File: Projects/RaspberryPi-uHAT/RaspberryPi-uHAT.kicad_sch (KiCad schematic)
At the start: 6 parts, among them J1 GPIO, U1 CAT24C256

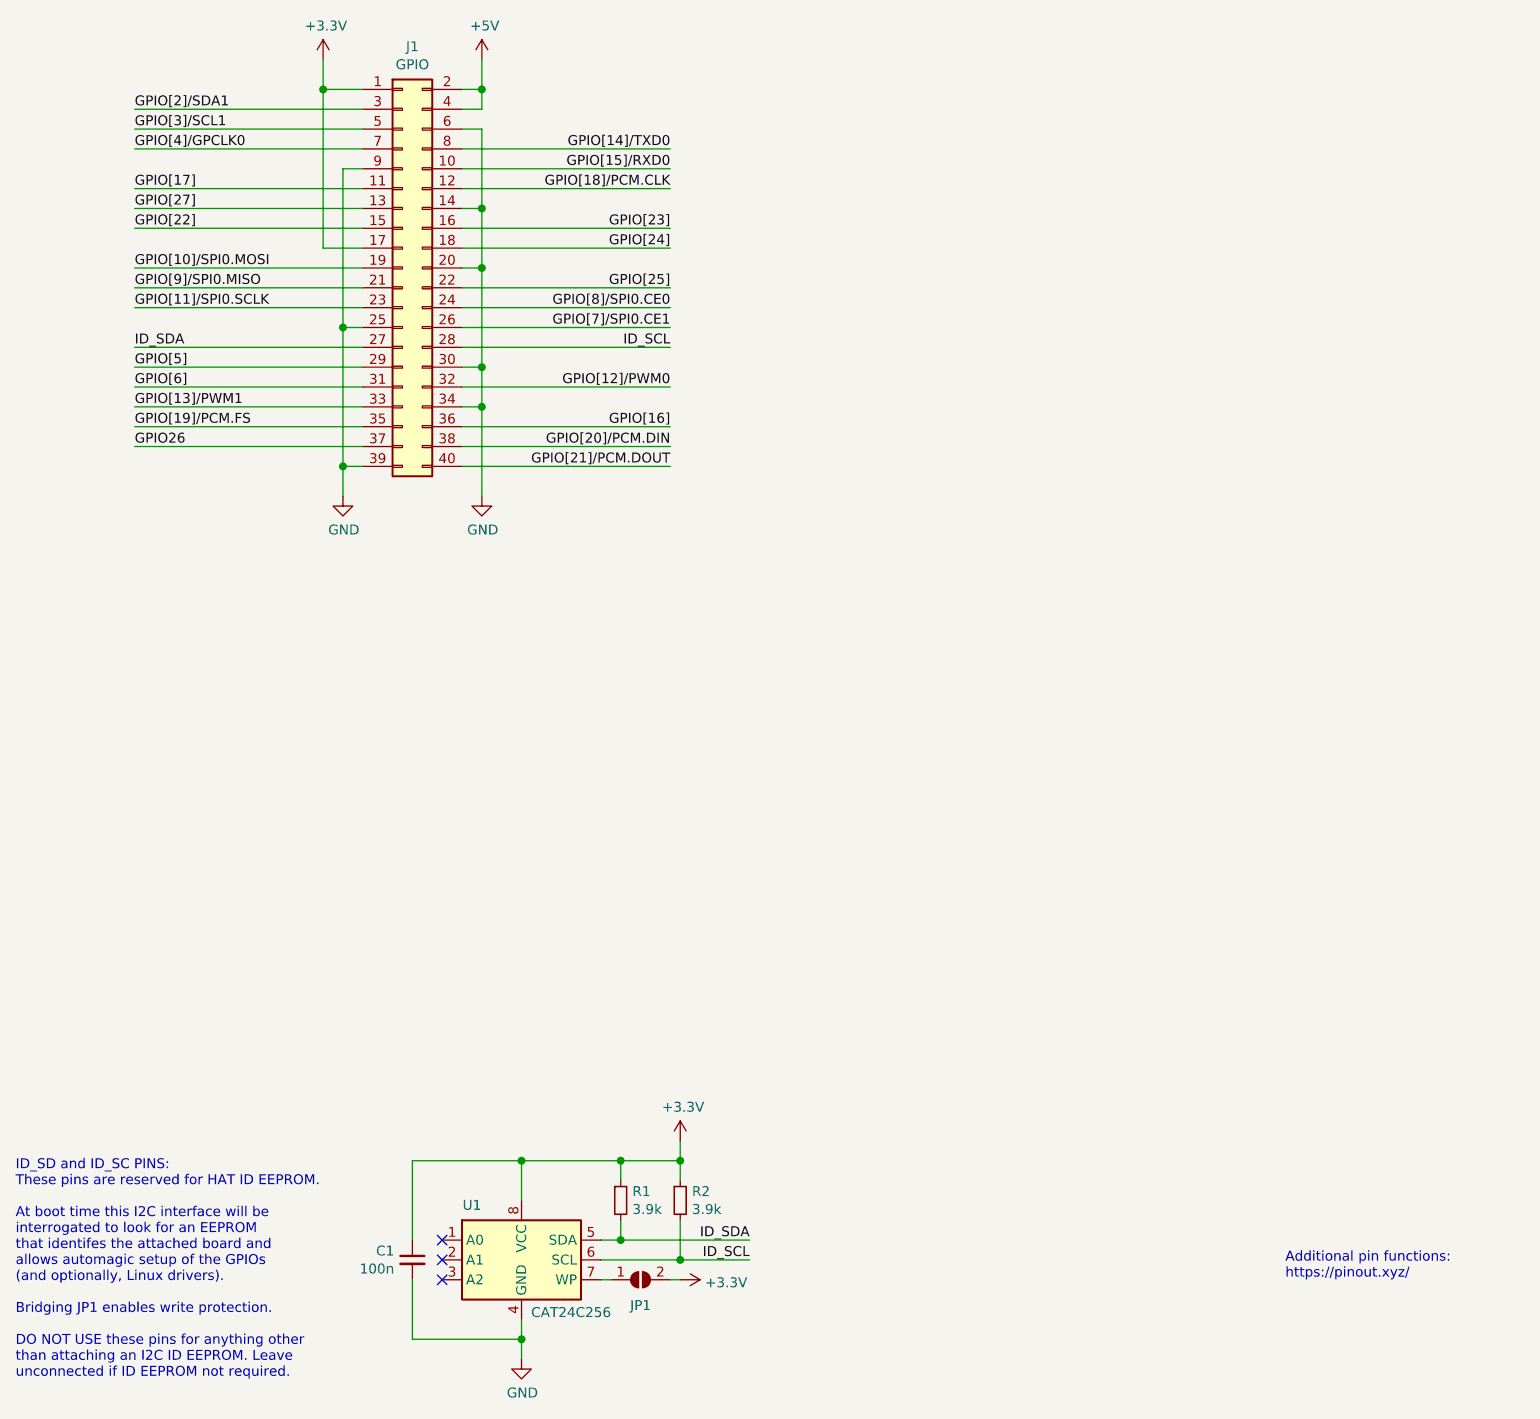
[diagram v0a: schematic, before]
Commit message: Update projects for KiCad version 7
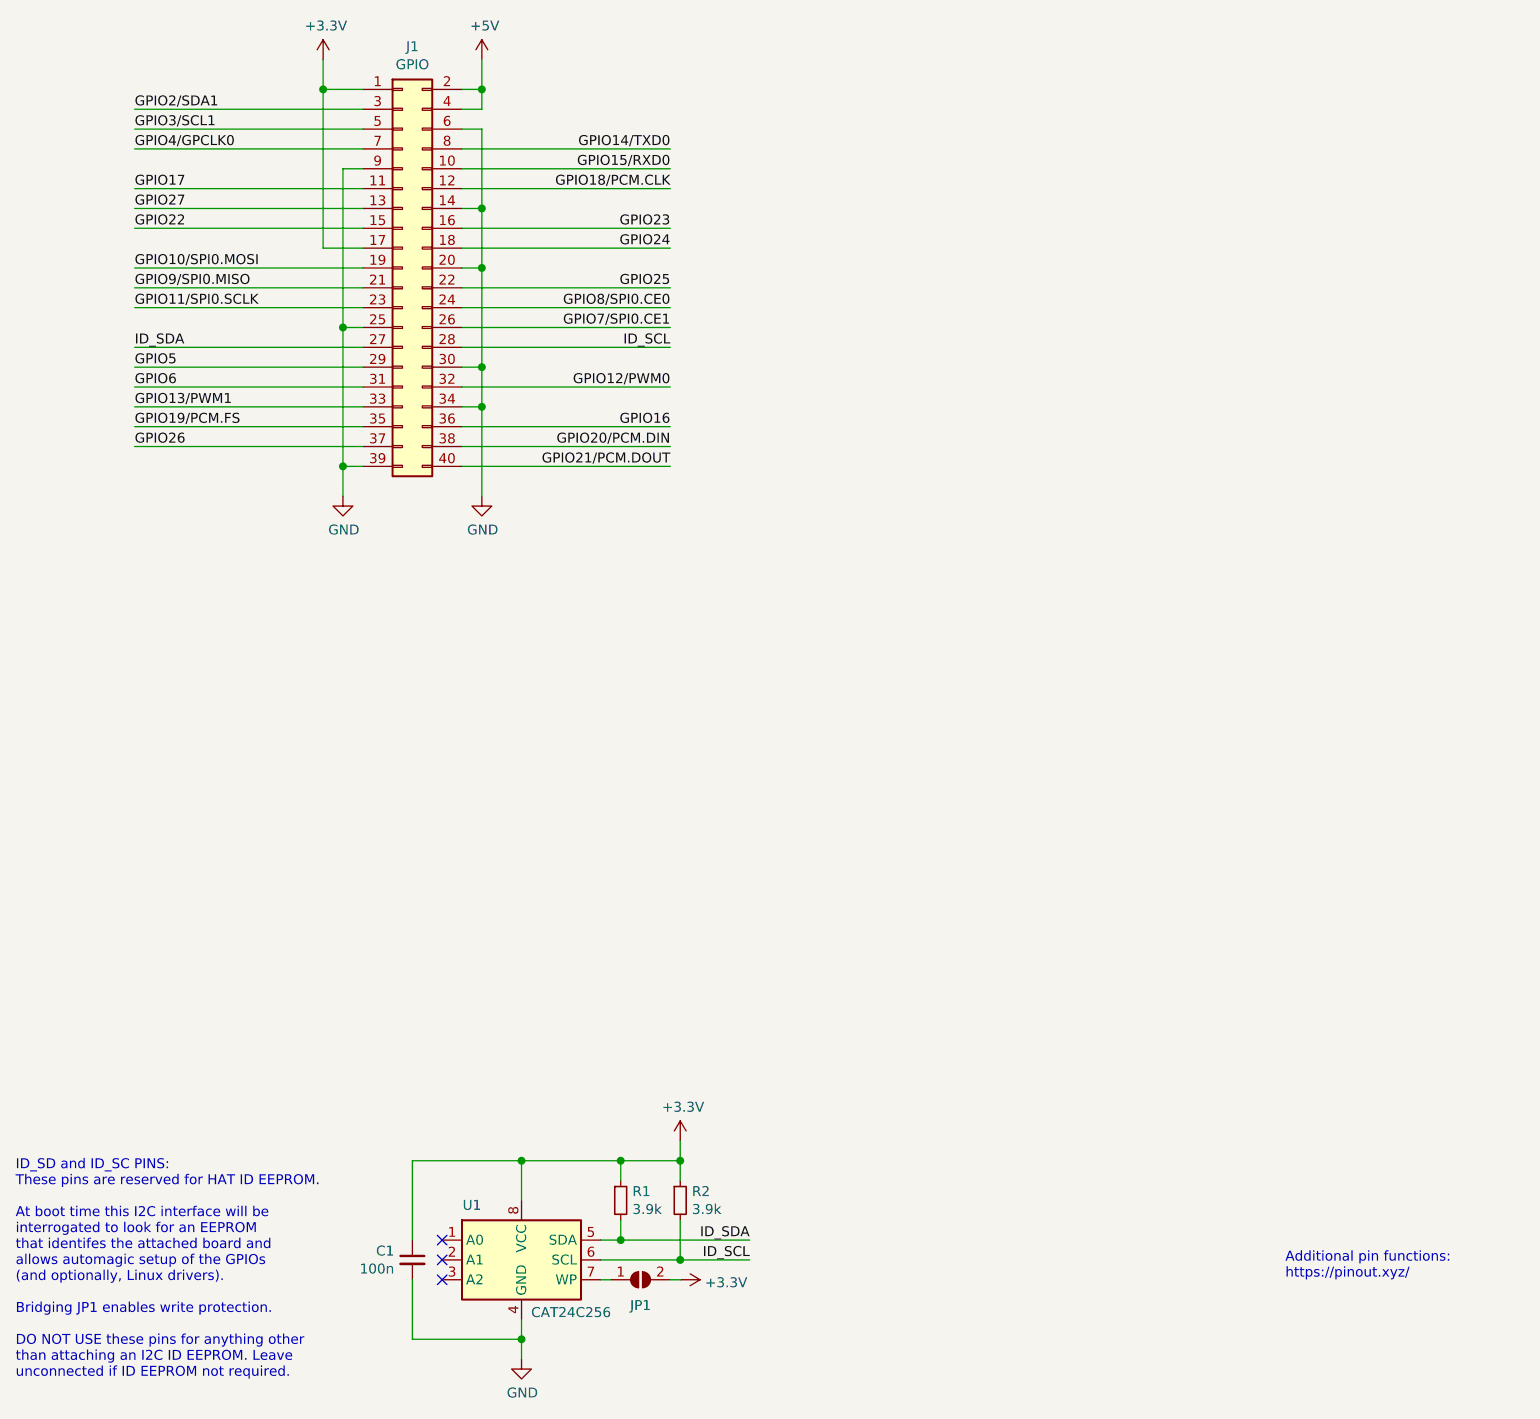
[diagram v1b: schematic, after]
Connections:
- net GPIO[10]/SPI0.MOSI renamed GPIO10/SPI0.MOSI
- net GPIO[11]/SPI0.SCLK renamed GPIO11/SPI0.SCLK
- net GPIO[12]/PWM0 renamed GPIO12/PWM0
- net GPIO[13]/PWM1 renamed GPIO13/PWM1
- net GPIO[14]/TXD0 renamed GPIO14/TXD0
- net GPIO[15]/RXD0 renamed GPIO15/RXD0
- net GPIO[16] renamed GPIO16
- net GPIO[17] renamed GPIO17
- net GPIO[18]/PCM.CLK renamed GPIO18/PCM.CLK
- net GPIO[19]/PCM.FS renamed GPIO19/PCM.FS
- net GPIO[20]/PCM.DIN renamed GPIO20/PCM.DIN
- net GPIO[21]/PCM.DOUT renamed GPIO21/PCM.DOUT
- net GPIO[22] renamed GPIO22
- net GPIO[23] renamed GPIO23
- net GPIO[24] renamed GPIO24
- net GPIO[25] renamed GPIO25
- net GPIO[27] renamed GPIO27
- net GPIO[2]/SDA1 renamed GPIO2/SDA1
- net GPIO[3]/SCL1 renamed GPIO3/SCL1
- net GPIO[4]/GPCLK0 renamed GPIO4/GPCLK0
- net GPIO[5] renamed GPIO5
- net GPIO[6] renamed GPIO6
- net GPIO[7]/SPI0.CE1 renamed GPIO7/SPI0.CE1
- net GPIO[8]/SPI0.CE0 renamed GPIO8/SPI0.CE0
- net GPIO[9]/SPI0.MISO renamed GPIO9/SPI0.MISO

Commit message: Update templates to V8 format
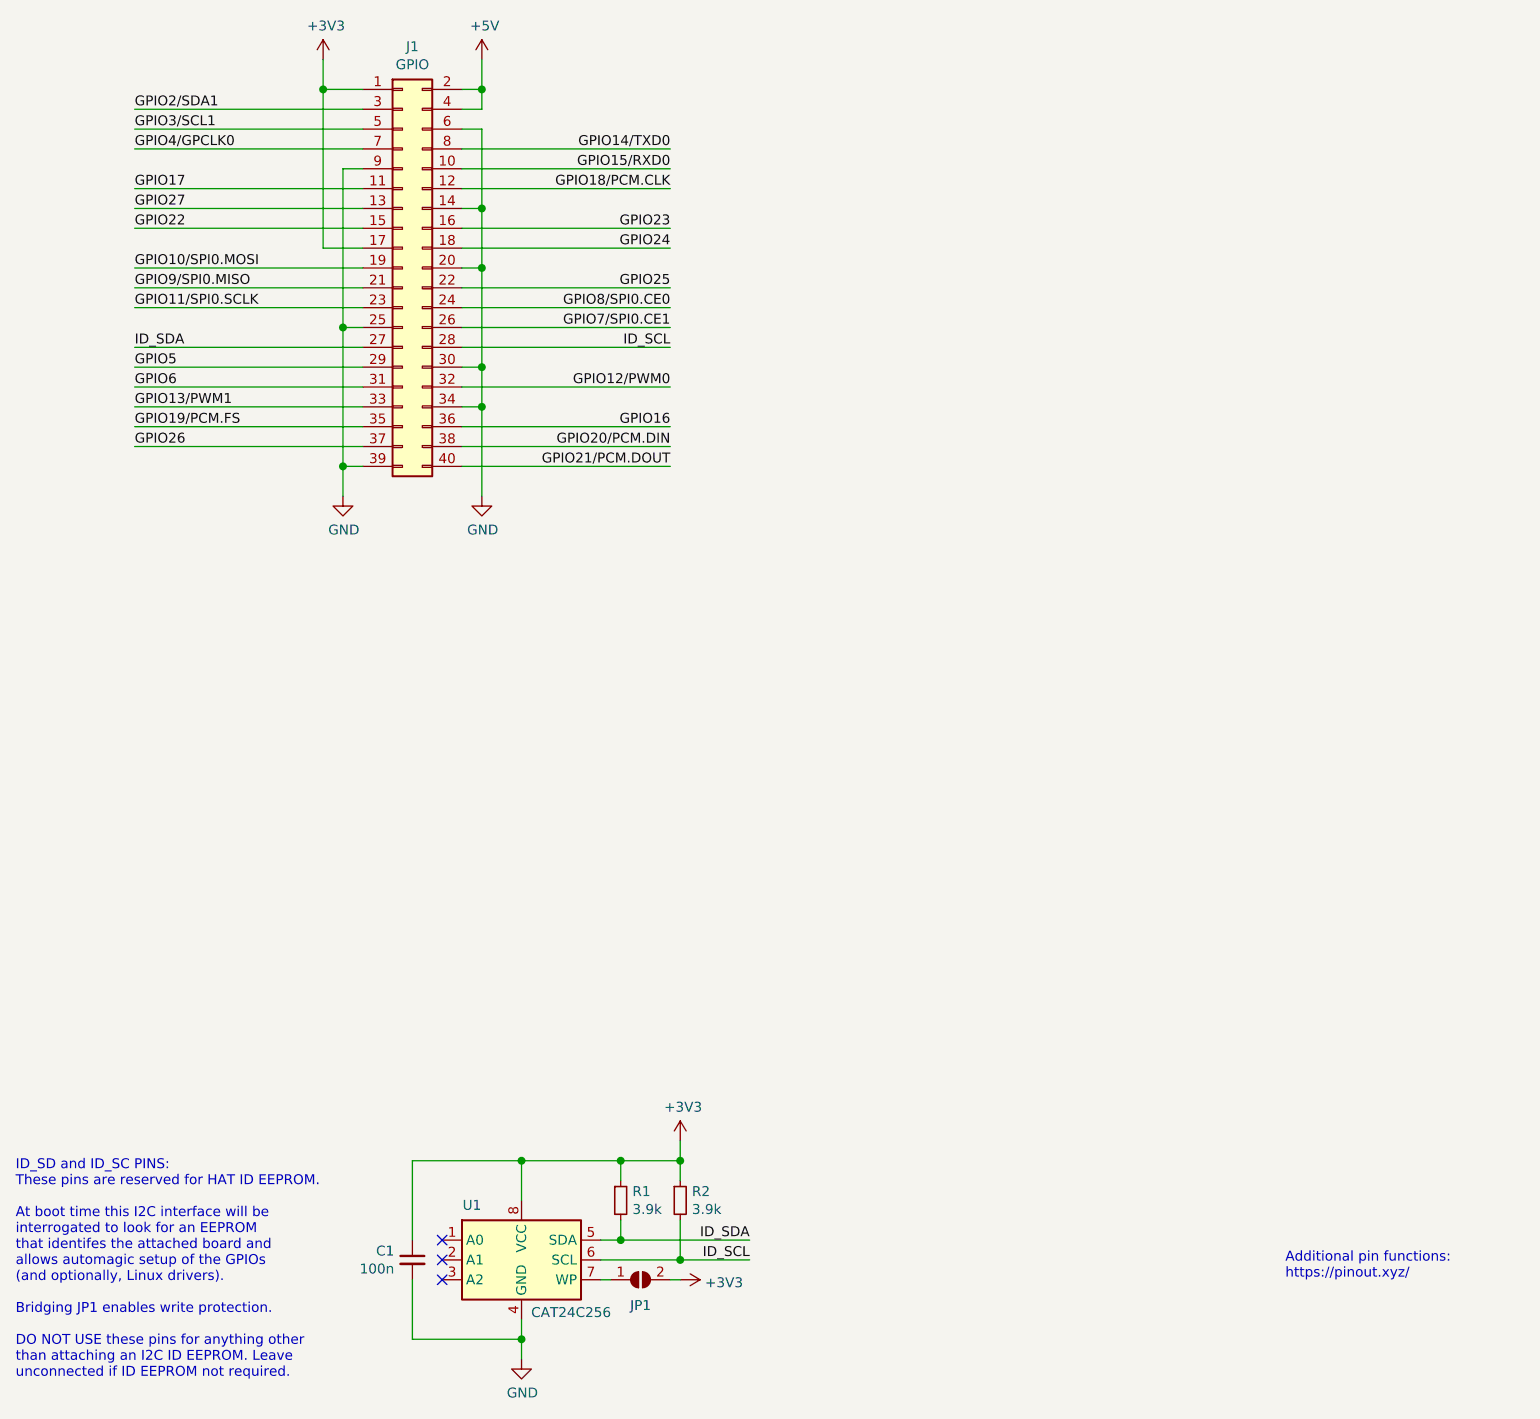
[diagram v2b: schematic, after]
